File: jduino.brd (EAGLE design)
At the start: 58.1 x 66 mm, 18 parts, among them IC1 LM2936Z-5.0, IC2 ATMEGA48/88/168-PU, J1 Analog I/O, J2 Digital I/O, J3 Digital I/O, J5 Power Jumpers, J6 FTDI Jumpers, Q1 16 mHz

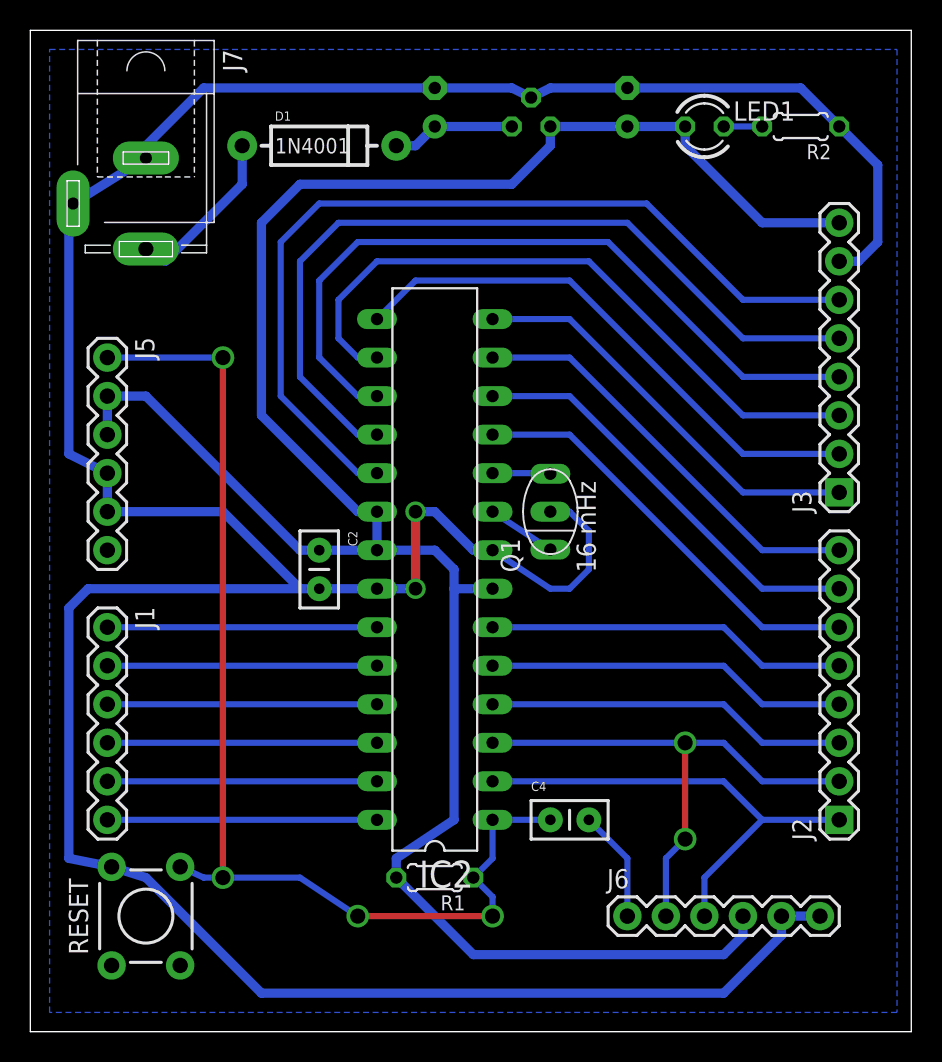
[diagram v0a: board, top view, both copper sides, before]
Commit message: Initial attempt at hand routing.
The ATmega needs to be moved to the left to allow enough space to
route all of the digital I/O pins.
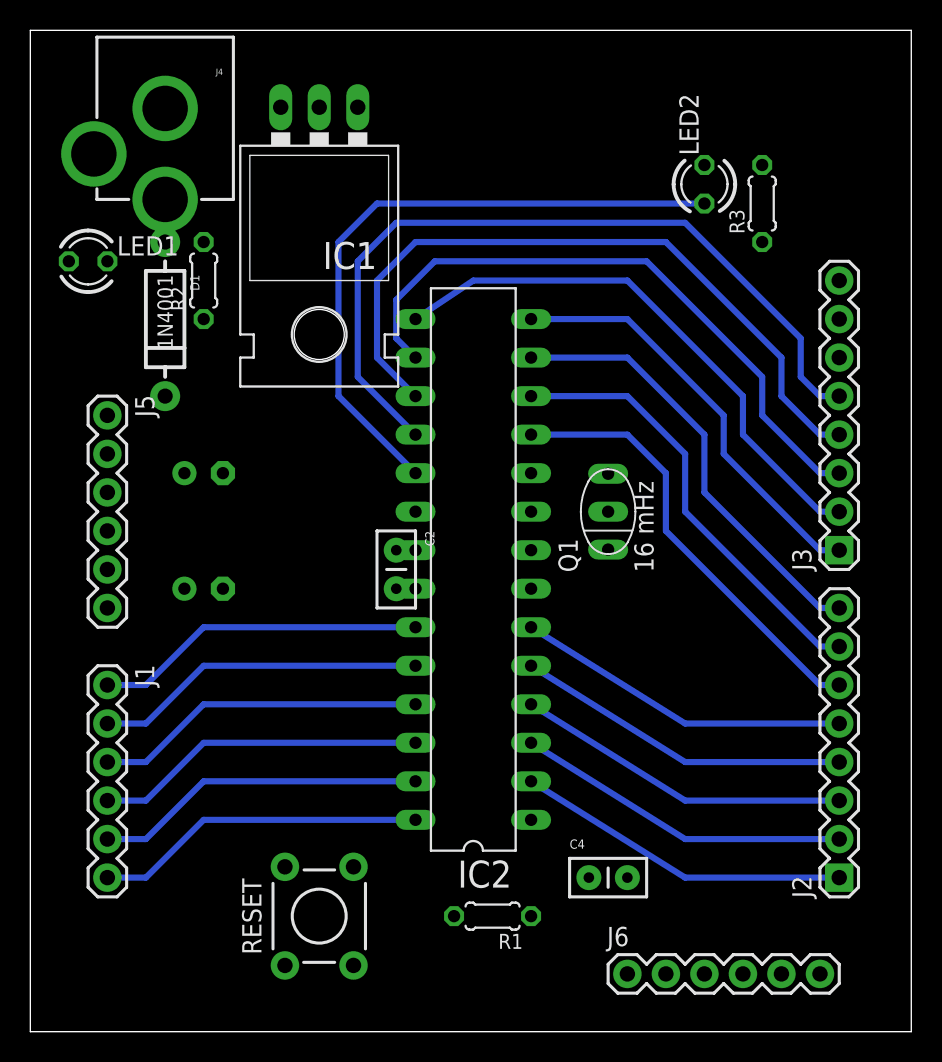
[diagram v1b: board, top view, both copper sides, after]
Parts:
- removed J7: (no value), con-jack:SPC4078
- added J4: POWER_JACKPTH, SparkFun-Connectors:POWER_JACK_PTH
- added LED2: LED13, led:LED3MM
- added R3: 330, rcl:0204/5
- IC1: value LM2936Z-5.0 -> LM2937-5.0; device national-semiconductor:TO92 -> SparkFun-PowerIC:TO-220-ALT
- moved C1 42.3 mm to (11.4, 29.2), turned to 180 degrees
- moved LED1 41.6 mm to (3.81, 50.8)
- moved R2 40.7 mm to (11.4, 49.5), turned to 90 degrees
- moved C3 28.5 mm to (11.4, 36.8), turned to 180 degrees
- moved D1 15.3 mm to (8.89, 47.0), turned to 270 degrees
- moved IC1 14.2 mm to (19.1, 57.1), flipped to the top, turned to 180 degrees
- moved RESET 11.4 mm to (19.1, 7.62)
- moved C2 5.08 mm to (24.1, 31.8)
- moved C4 4.58 mm to (36.8, 10.2)
- moved R1 4.58 mm to (30.5, 7.62)
- moved J1 3.81 mm to (5.08, 22.9)
- moved J3 3.81 mm to (53.3, 31.8)
- moved J5 3.81 mm to (5.08, 40.6)
- moved Q1 3.81 mm to (38.1, 34.3)
- moved J2 3.81 mm to (53.3, 10.2)
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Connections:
- new net N$4: LED2.K, R3.2
- net +5V: now also IC1.OUT; no longer IC1.1
- net D13: now also LED2.A
- net GND: now also IC1.GND, J4.GNDBREAK, R3.1; no longer IC1.2, J7.1, J7.2
- net N$2: now also J4.PWR; no longer J7.3
- net N$6: now also IC1.IN; no longer IC1.3
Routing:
- net GND: track 223.9 -> 0.00 mm, vias 2 -> 0
- net +5V: track 152.1 -> 0.00 mm
- net RESET: track 74.6 -> 0.00 mm, vias 4 -> 0
- net D13: track 59.1 -> 42.5 mm
- net D1: track 35.9 -> 22.1 mm, vias 2 -> 0
- net D0: track 31.8 -> 22.1 mm
- net N$2: track 11.2 -> 2.81 mm
- net N$6: track 8.15 -> 0.00 mm
- net N$1: track 7.40 -> 0.00 mm
- net N$5: track 4.56 -> 0.00 mm
- net A5: track 17.8 -> 21.9 mm
- net A4: track 17.8 -> 21.9 mm
- net A3: track 17.8 -> 21.9 mm
- net A2: track 17.8 -> 21.9 mm
- net A1: track 17.8 -> 21.9 mm
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- removed copper zone on layer 16, net GND
